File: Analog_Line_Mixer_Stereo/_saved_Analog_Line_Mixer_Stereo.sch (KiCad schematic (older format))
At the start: 37 parts, among them J1 IN-1, J2 IN-2, J3 IN-3, J4 IN-4

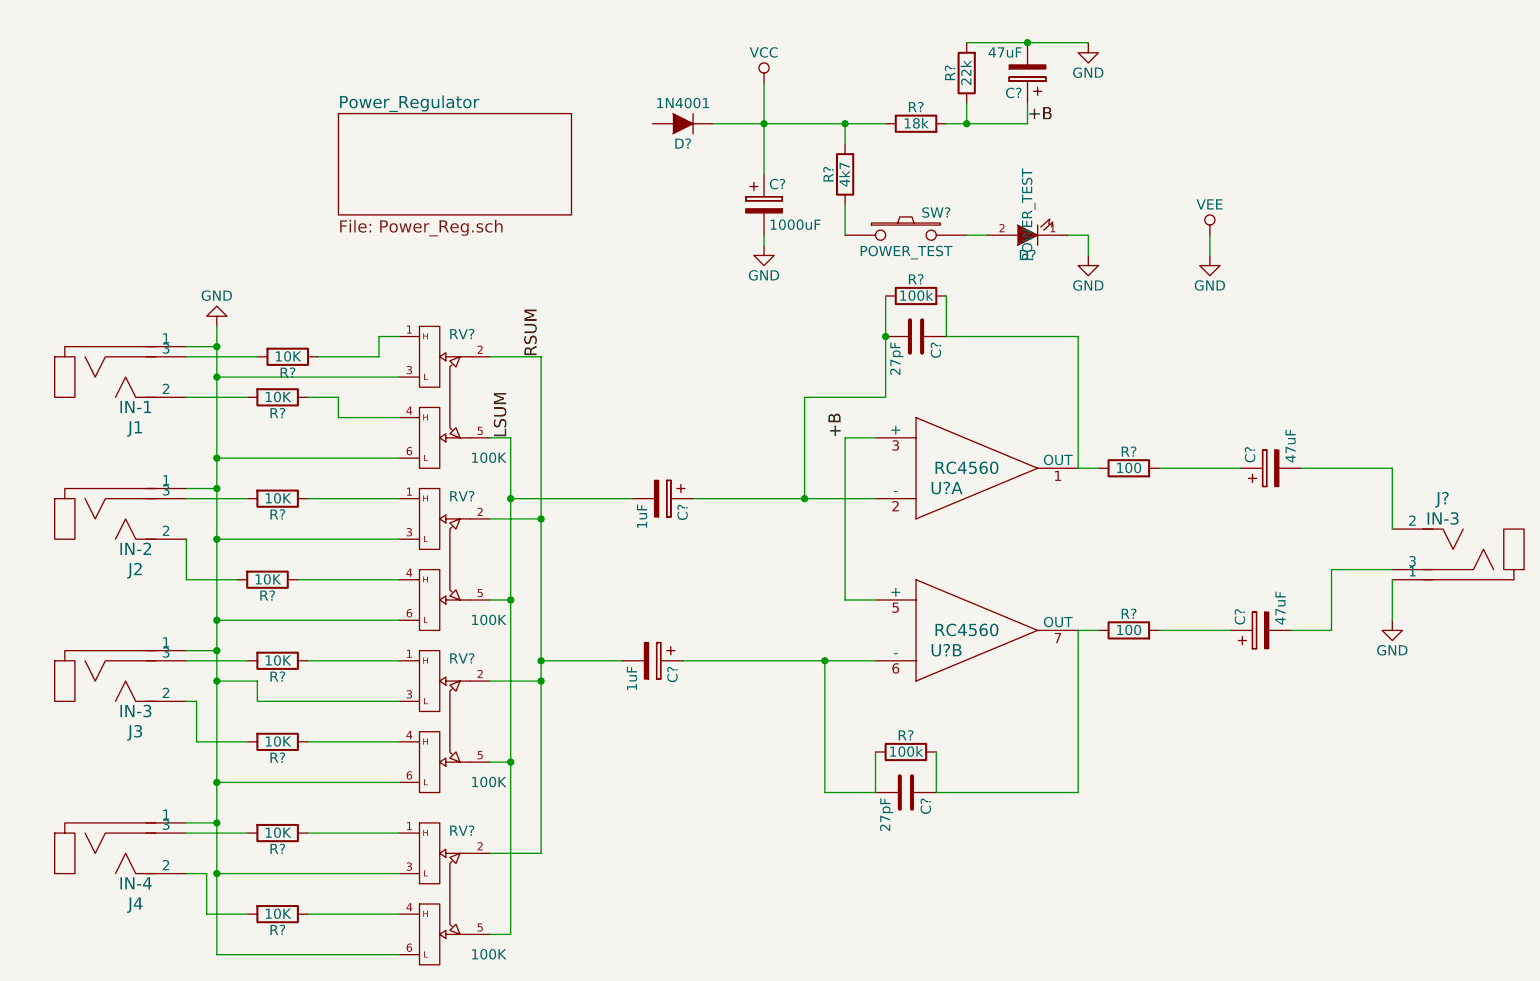
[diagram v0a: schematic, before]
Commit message: adding switches and power sources
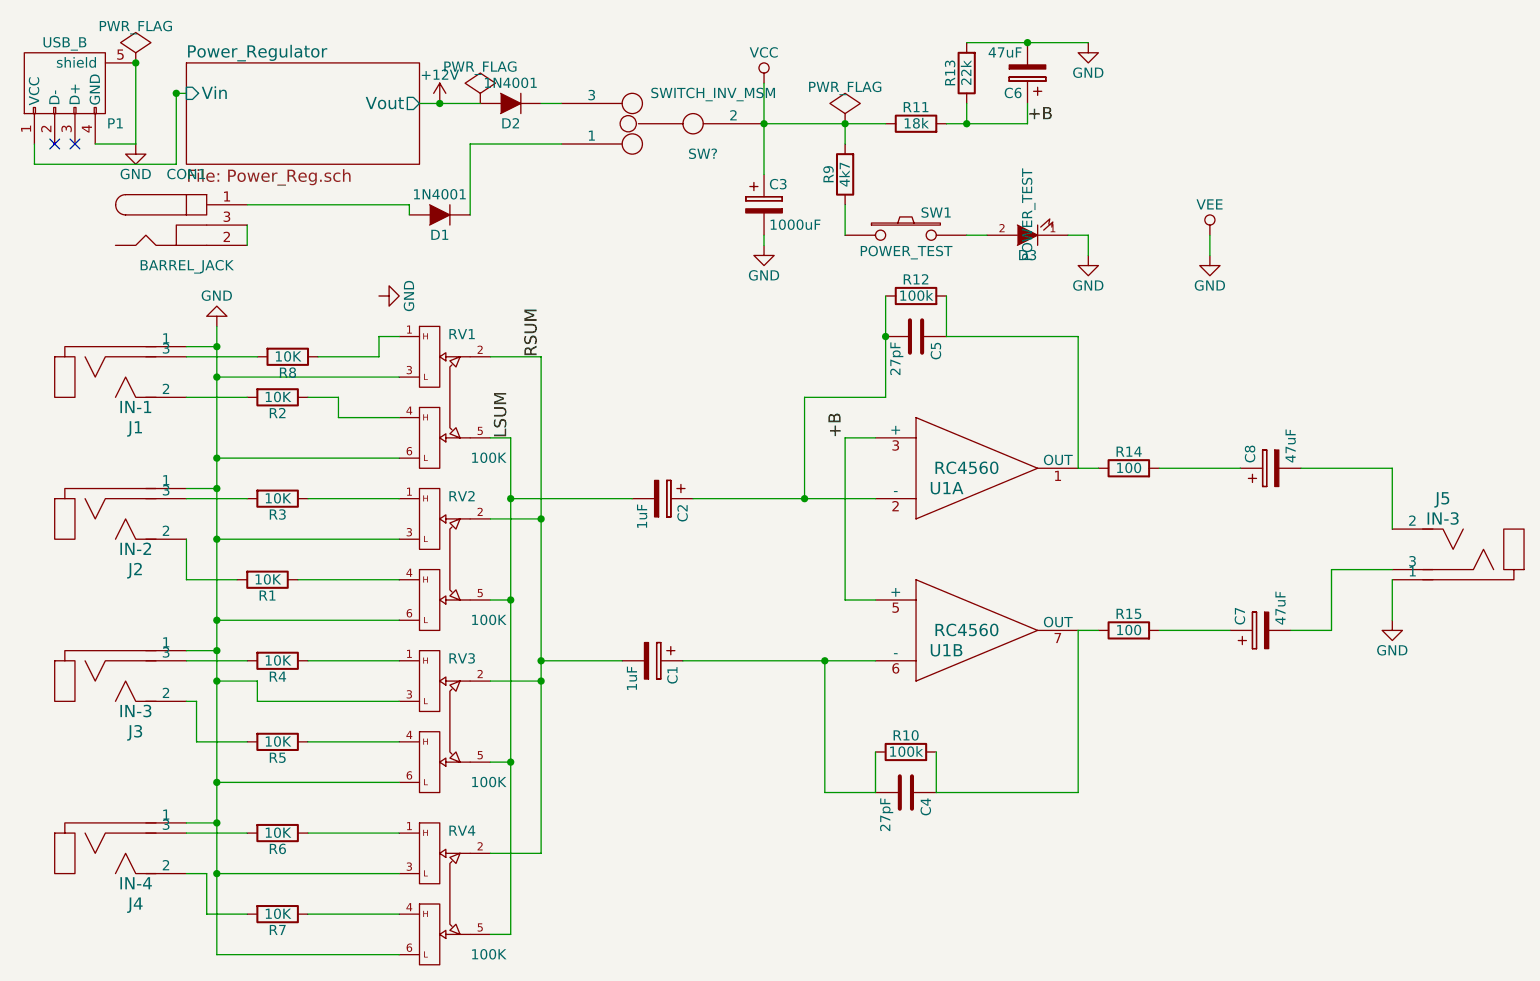
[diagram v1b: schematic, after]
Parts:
- added CON1: BARREL_JACK, symbol BARREL_JACK
- added D1: 1N4001, symbol D
- added P1: USB_B, symbol USB_B
- added SW?: SWITCH_INV_MSM, symbol SWITCH_INV_MSM
- C1, C2, C3, C4, C5, C6, C7, C8: renamed from C?; footprint (none) -> Capacitors_SMD:C_1206
- D3: renamed from D?; footprint (none) -> LEDs:LED_0805
- R1, R10, R11, R12, R13, R14, R15, R2, R3, R4, R5, R6, R7, R8, R9: renamed from R?; footprint Resistors_SMD:R_1206 -> (none)
- gave numbers to parts that had none: 8
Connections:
- net GND: now also P1.4 (GND), P1.5 (shield)
- net VCC: now also SW?.2; no longer D2.1 (K)
- net +12V: now reaches D2.2 (A)
- new net: D2.1 (K), SW?.3
- new net: D1.1 (K), SW?.1
- new net: CON1.1, D1.2 (A)
- new net: CON1.2, CON1.3
- new net Power_Regulator/Vin: P1.1 (VCC)
- no-connect marks 0 -> 2
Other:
- moved on the sheet: D2

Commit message: finalized schematic and started on board
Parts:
- CON1: footprint (none) -> CUI-INC:Barrel_Jack_2.1x5.5mm_CUI_INC
- D1, D2: footprint (none) -> Diodes_SMD:SOD-323
- D3: footprint LEDs:LED_0805 -> LEDs:LED_0603
- J1, J2, J3, J4: footprint (none) -> CUI-INC:SJ1-353XNG-5Pin
- J5: value IN-3 -> OUT; footprint (none) -> CUI-INC:SJ1-353XNG-5Pin
- P1: footprint (none) -> Connect:USB_Micro-B
- R1, R10, R11, R12, R13, R14, R15, R2, R3, R4, R5, R6, R7, R8: footprint (none) -> Resistors_SMD:R_1206
- R9: value 4k7 -> 2k; footprint (none) -> Resistors_SMD:R_1206
- RV1, RV2, RV3, RV4: footprint (none) -> Taiwan_Alpha:TA-Dual-Pot-pin-RV122F
- SW2: renamed from SW?; value SWITCH_INV_MSM -> Power Selector; footprint (none) -> Grayhill:Grayhill-47B-switches-SPDT-M6
- U1: footprint (none) -> TI-R-PDSO-G8:TI-LM2698-MUA08A
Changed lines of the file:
@@
 F 0 "J1" H 1400 2350 60  0000 C CNN
 F 1 "IN-1" H 1400 2450 60  0000 C CNN
-F 2 "" H 1400 2450 60  0001 C CNN
+F 2 "CUI-INC:SJ1-353XNG-5Pin" H 1400 2450 60  0001 C CNN
 F 3 "" H 1400 2450 60  0000 C CNN
 	1    1400 2450
@@
 F 0 "J2" H 1400 3050 60  0000 C CNN
 F 1 "IN-2" H 1400 3150 60  0000 C CNN
-F 2 "" H 1400 3150 60  0001 C CNN
+F 2 "CUI-INC:SJ1-353XNG-5Pin" H 1400 3150 60  0001 C CNN
 F 3 "" H 1400 3150 60  0000 C CNN
 	1    1400 3150
@@
 F 0 "J3" H 1400 3850 60  0000 C CNN
 F 1 "IN-3" H 1400 3950 60  0000 C CNN
-F 2 "" H 1400 3950 60  0001 C CNN
+F 2 "CUI-INC:SJ1-353XNG-5Pin" H 1400 3950 60  0001 C CNN
 F 3 "" H 1400 3950 60  0000 C CNN
 	1    1400 3950
@@
 F 0 "J4" H 1400 4700 60  0000 C CNN
 F 1 "IN-4" H 1400 4800 60  0000 C CNN
-F 2 "" H 1400 4800 60  0001 C CNN
+F 2 "CUI-INC:SJ1-353XNG-5Pin" H 1400 4800 60  0001 C CNN
 F 3 "" H 1400 4800 60  0000 C CNN
 	1    1400 4800
@@
 F 0 "RV1" H 3010 2710 50  0000 C CNN
 F 1 "100K" H 3140 2100 50  0000 C CNN
-F 2 "" H 2850 2400 50  0001 C CNN
+F 2 "Taiwan_Alpha:TA-Dual-Pot-pin-RV122F" H 2850 2400 50  0001 C CNN
 F 3 "" H 2850 2400 50  0000 C CNN
 	1    2850 2400
@@
 F 0 "RV2" H 3010 3510 50  0000 C CNN
 F 1 "100K" H 3140 2900 50  0000 C CNN
-F 2 "" H 2850 3200 50  0001 C CNN
+F 2 "Taiwan_Alpha:TA-Dual-Pot-pin-RV122F" H 2850 3200 50  0001 C CNN
 F 3 "" H 2850 3200 50  0000 C CNN
 	1    2850 3200
@@
 F 0 "RV3" H 3010 4310 50  0000 C CNN
 F 1 "100K" H 3140 3700 50  0000 C CNN
-F 2 "" H 2850 4000 50  0001 C CNN
+F 2 "Taiwan_Alpha:TA-Dual-Pot-pin-RV122F" H 2850 4000 50  0001 C CNN
 F 3 "" H 2850 4000 50  0000 C CNN
 	1    2850 4000
@@
 F 0 "RV4" H 3010 5160 50  0000 C CNN
 F 1 "100K" H 3140 4550 50  0000 C CNN
-F 2 "" H 2850 4850 50  0001 C CNN
+F 2 "Taiwan_Alpha:TA-Dual-Pot-pin-RV122F" H 2850 4850 50  0001 C CNN
 F 3 "" H 2850 4850 50  0000 C CNN
 	1    2850 4850
@@
 F 0 "R8" V 2230 2200 50  0000 C CNN
 F 1 "10K" V 2150 2200 50  0000 C CNN
-F 2 "" V 2080 2200 50  0001 C CNN
+F 2 "Resistors_SMD:R_1206" V 2080 2200 50  0001 C CNN
 F 3 "" H 2150 2200 50  0000 C CNN
 	1    2150 2200
@@
 F 0 "R2" V 2180 2400 50  0000 C CNN
 F 1 "10K" V 2100 2400 50  0000 C CNN
-F 2 "" V 2030 2400 50  0001 C CNN
+F 2 "Resistors_SMD:R_1206" V 2030 2400 50  0001 C CNN
 F 3 "" H 2100 2400 50  0000 C CNN
 	1    2100 2400
@@
 F 0 "R3" V 2180 2900 50  0000 C CNN
 F 1 "10K" V 2100 2900 50  0000 C CNN
-F 2 "" V 2030 2900 50  0001 C CNN
+F 2 "Resistors_SMD:R_1206" V 2030 2900 50  0001 C CNN
 F 3 "" H 2100 2900 50  0000 C CNN
 	1    2100 2900
@@
 F 0 "R1" V 2130 3300 50  0000 C CNN
 F 1 "10K" V 2050 3300 50  0000 C CNN
-F 2 "" V 1980 3300 50  0001 C CNN
+F 2 "Resistors_SMD:R_1206" V 1980 3300 50  0001 C CNN
 F 3 "" H 2050 3300 50  0000 C CNN
 	1    2050 3300
@@
 F 0 "R4" V 2180 3700 50  0000 C CNN
 F 1 "10K" V 2100 3700 50  0000 C CNN
-F 2 "" V 2030 3700 50  0001 C CNN
+F 2 "Resistors_SMD:R_1206" V 2030 3700 50  0001 C CNN
 F 3 "" H 2100 3700 50  0000 C CNN
 	1    2100 3700
@@
 F 0 "R5" V 2180 4100 50  0000 C CNN
 F 1 "10K" V 2100 4100 50  0000 C CNN
-F 2 "" V 2030 4100 50  0001 C CNN
+F 2 "Resistors_SMD:R_1206" V 2030 4100 50  0001 C CNN
 F 3 "" H 2100 4100 50  0000 C CNN
 	1    2100 4100
@@
 F 0 "R6" V 2180 4550 50  0000 C CNN
 F 1 "10K" V 2100 4550 50  0000 C CNN
-F 2 "" V 2030 4550 50  0001 C CNN
+F 2 "Resistors_SMD:R_1206" V 2030 4550 50  0001 C CNN
 F 3 "" H 2100 4550 50  0000 C CNN
 	1    2100 4550
@@
 F 0 "R7" V 2180 4950 50  0000 C CNN
 F 1 "10K" V 2100 4950 50  0000 C CNN
-F 2 "" V 2030 4950 50  0001 C CNN
+F 2 "Resistors_SMD:R_1206" V 2030 4950 50  0001 C CNN
 F 3 "" H 2100 4950 50  0000 C CNN
 	1    2100 4950
@@
 F 0 "U1" H 5400 2650 60  0000 C CNN
 F 1 "RC4560" H 5500 2750 60  0000 C CNN
-F 2 "" H 5500 2750 60  0001 C CNN
+F 2 "TI-R-PDSO-G8:TI-LM2698-MUA08A" H 5500 2750 60  0001 C CNN
 F 3 "" H 5500 2750 60  0000 C CNN
 	1    5450 2750
@@
 F 0 "U1" H 5400 3450 60  0000 C CNN
 F 1 "RC4560" H 5500 3550 60  0000 C CNN
-F 2 "" H 5500 3550 60  0001 C CNN
+F 2 "TI-R-PDSO-G8:TI-LM2698-MUA08A" H 5500 3550 60  0001 C CNN
 F 3 "" H 5500 3550 60  0000 C CNN
 	2    5450 3550
@@
 F 0 "D2" H 3250 1050 50  0000 C CNN
 F 1 "1N4001" H 3250 850 50  0000 C CNN
-F 2 "" H 3250 950 50  0001 C CNN
+F 2 "Diodes_SMD:SOD-323" H 3250 950 50  0001 C CNN
 F 3 "" H 3250 950 50  0000 C CNN
 	1    3250 950
@@
 P 4900 1300
 F 0 "R9" V 4980 1300 50  0000 C CNN
-F 1 "4k7" V 4900 1300 50  0000 C CNN
-F 2 "" V 4830 1300 50  0001 C CNN
+F 1 "2k" V 4900 1300 50  0000 C CNN
+F 2 "Resistors_SMD:R_1206" V 4830 1300 50  0001 C CNN
 F 3 "" H 4900 1300 50  0000 C CNN
 	1    4900 1300
@@
 F 0 "D3" H 5800 1700 50  0000 C CNN
 F 1 "POWER_TEST" V 5800 1500 50  0000 C CNN
-F 2 "LEDs:LED_0805" H 5800 1600 50  0001 C CNN
+F 2 "LEDs:LED_0603" H 5800 1600 50  0001 C CNN
 F 3 "" H 5800 1600 50  0000 C CNN
 	1    5800 1600
@@
 F 0 "R11" V 5330 1050 50  0000 C CNN
 F 1 "18k" V 5250 1050 50  0000 C CNN
-F 2 "" V 5180 1050 50  0001 C CNN
+F 2 "Resistors_SMD:R_1206" V 5180 1050 50  0001 C CNN
 F 3 "" H 5250 1050 50  0000 C CNN
 	1    5250 1050
@@
 F 0 "R13" V 5580 800 50  0000 C CNN
 F 1 "22k" V 5500 800 50  0000 C CNN
-F 2 "" V 5430 800 50  0001 C CNN
+F 2 "Resistors_SMD:R_1206" V 5430 800 50  0001 C CNN
 F 3 "" H 5500 800 50  0000 C CNN
 	1    5500 800
@@
 F 0 "R12" V 5330 1900 50  0000 C CNN
 F 1 "100k" V 5250 1900 50  0000 C CNN
-F 2 "" V 5180 1900 50  0001 C CNN
+F 2 "Resistors_SMD:R_1206" V 5180 1900 50  0001 C CNN
 F 3 "" H 5250 1900 50  0000 C CNN
 	1    5250 1900
@@
 F 0 "R10" V 5280 4150 50  0000 C CNN
 F 1 "100k" V 5200 4150 50  0000 C CNN
-F 2 "" V 5130 4150 50  0001 C CNN
+F 2 "Resistors_SMD:R_1206" V 5130 4150 50  0001 C CNN
 F 3 "" H 5200 4150 50  0000 C CNN
 	1    5200 4150
@@
 F 0 "R14" V 6380 2750 50  0000 C CNN
 F 1 "100" V 6300 2750 50  0000 C CNN
-F 2 "" V 6230 2750 50  0001 C CNN
+F 2 "Resistors_SMD:R_1206" V 6230 2750 50  0001 C CNN
 F 3 "" H 6300 2750 50  0000 C CNN
 	1    6300 2750
@@
 F 0 "R15" V 6380 3550 50  0000 C CNN
 F 1 "100" V 6300 3550 50  0000 C CNN
-F 2 "" V 6230 3550 50  0001 C CNN
+F 2 "Resistors_SMD:R_1206" V 6230 3550 50  0001 C CNN
 F 3 "" H 6300 3550 50  0000 C CNN
 	1    6300 3550
@@
 P 7850 3000
 F 0 "J5" H 7850 2900 60  0000 C CNN
-F 1 "IN-3" H 7850 3000 60  0000 C CNN
-F 2 "" H 7850 3000 60  0001 C CNN
+F 1 "OUT" H 7850 3000 60  0000 C CNN
+F 2 "CUI-INC:SJ1-353XNG-5Pin" H 7850 3000 60  0001 C CNN
 F 3 "" H 7850 3000 60  0000 C CNN
 	1    7850 3000
@@
 F 0 "P1" H 1300 650 50  0000 C CNN
 F 1 "USB_B" H 1050 1050 50  0000 C CNN
-F 2 "" V 1050 750 50  0001 C CNN
+F 2 "Connect:USB_Micro-B" V 1050 750 50  0001 C CNN
 F 3 "" V 1050 750 50  0000 C CNN
 	1    1100 850
@@
 F 0 "D1" H 2900 1600 50  0000 C CNN
 F 1 "1N4001" H 2900 1400 50  0000 C CNN
-F 2 "" H 2900 1500 50  0001 C CNN
+F 2 "Diodes_SMD:SOD-323" H 2900 1500 50  0001 C CNN
 F 3 "" H 2900 1500 50  0000 C CNN
 	1    2900 1500
@@
 F 0 "CON1" H 1650 1800 50  0000 C CNN
 F 1 "BARREL_JACK" H 1650 1350 50  0000 C CNN
-F 2 "" H 1650 1550 50  0001 C CNN
+F 2 "CUI-INC:Barrel_Jack_2.1x5.5mm_CUI_INC" H 1650 1550 50  0001 C CNN
 F 3 "" H 1650 1550 50  0000 C CNN
 	1    1650 1550
@@
 $EndComp
 $Comp
-L SWITCH_INV_MSM SW?
+L SWITCH_INV_MSM SW2
 U 1 1 56B84158
 P 4000 1050
-F 0 "SW?" H 3801 1200 50  0000 C CNN
-F 1 "SWITCH_INV_MSM" H 3750 900 50  0000 C CNN
-F 2 "" H 4000 1050 50  0000 C CNN
+F 0 "SW2" H 3801 1200 50  0000 C CNN
+F 1 "Power Selector" H 3750 900 50  0000 C CNN
+F 2 "Grayhill:Grayhill-47B-switches-SPDT-M6" H 4000 1050 50  0001 C CNN
 F 3 "" H 4000 1050 50  0000 C CNN
 	1    4000 1050
